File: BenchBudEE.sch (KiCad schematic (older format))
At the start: 0 parts

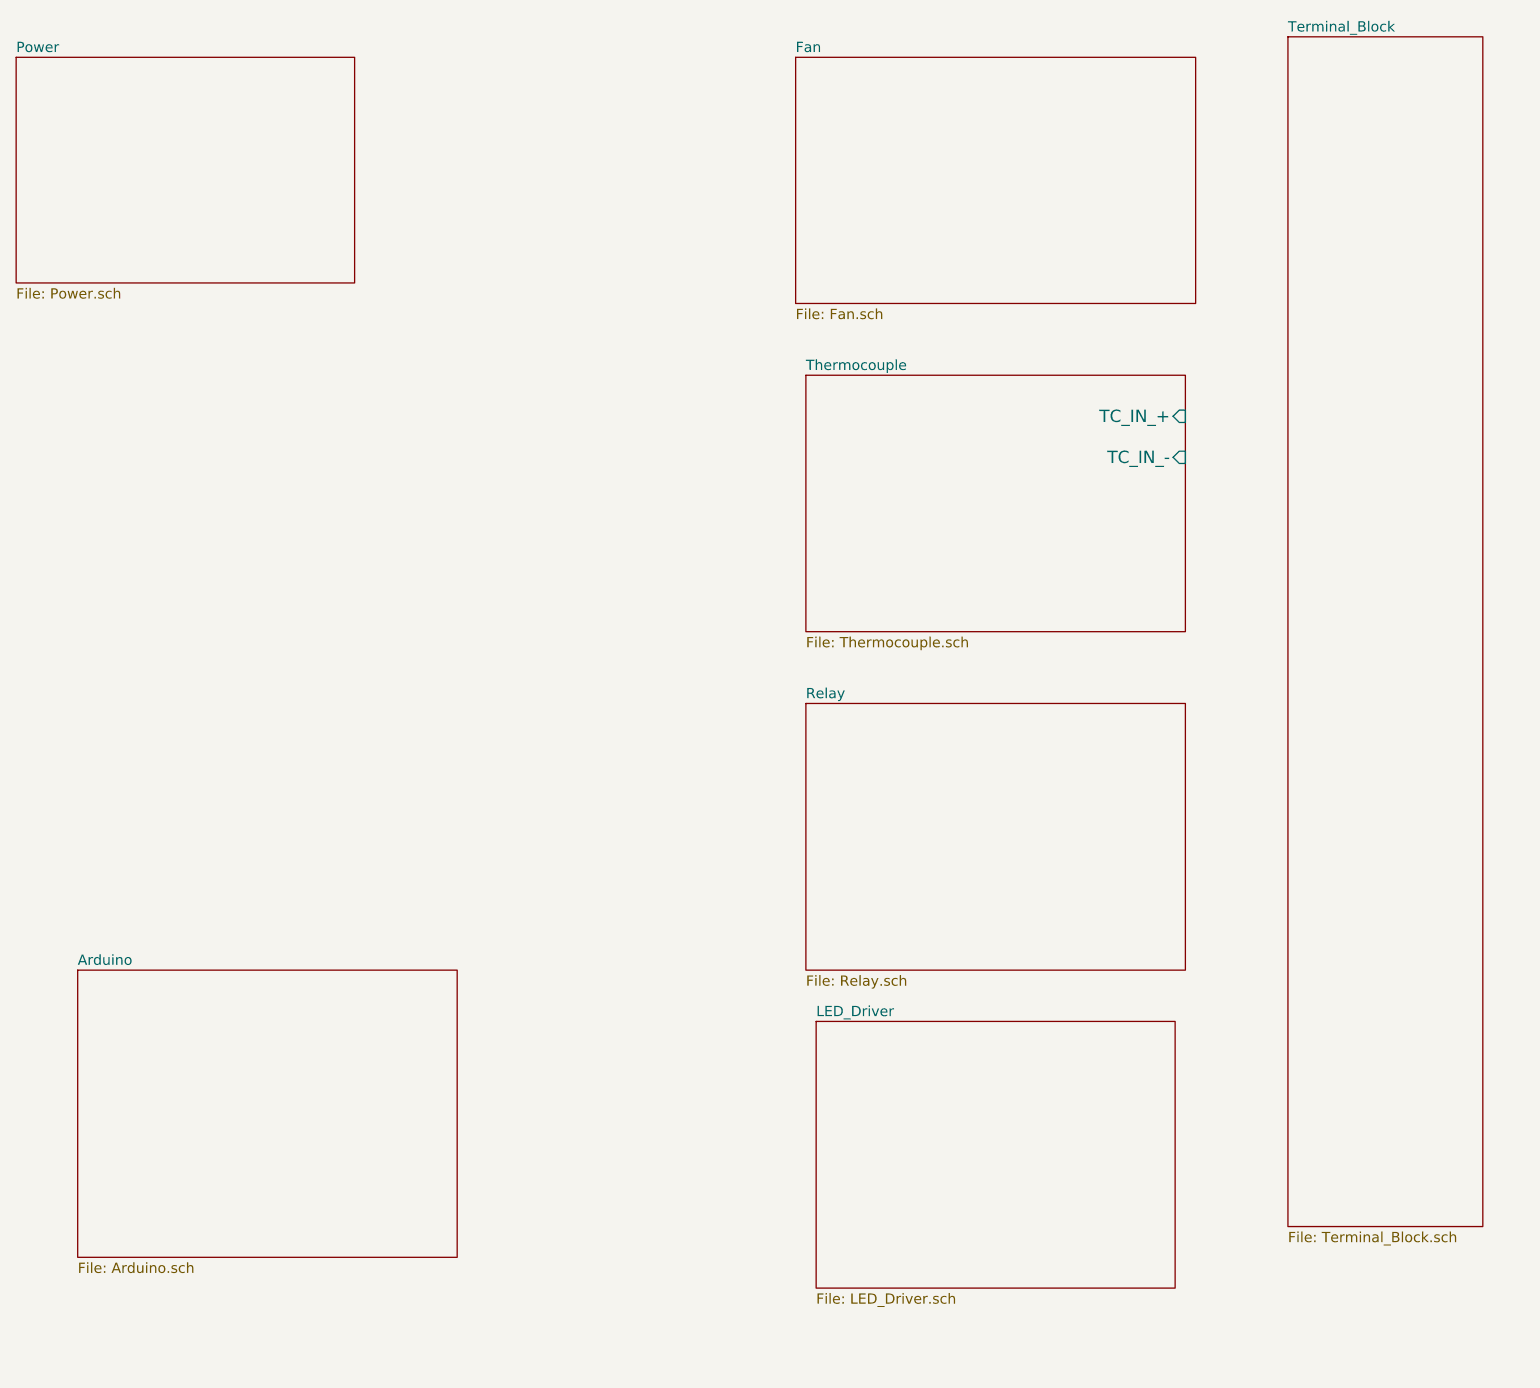
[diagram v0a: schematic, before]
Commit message: Created inputs/outputs in hierarchical sheets
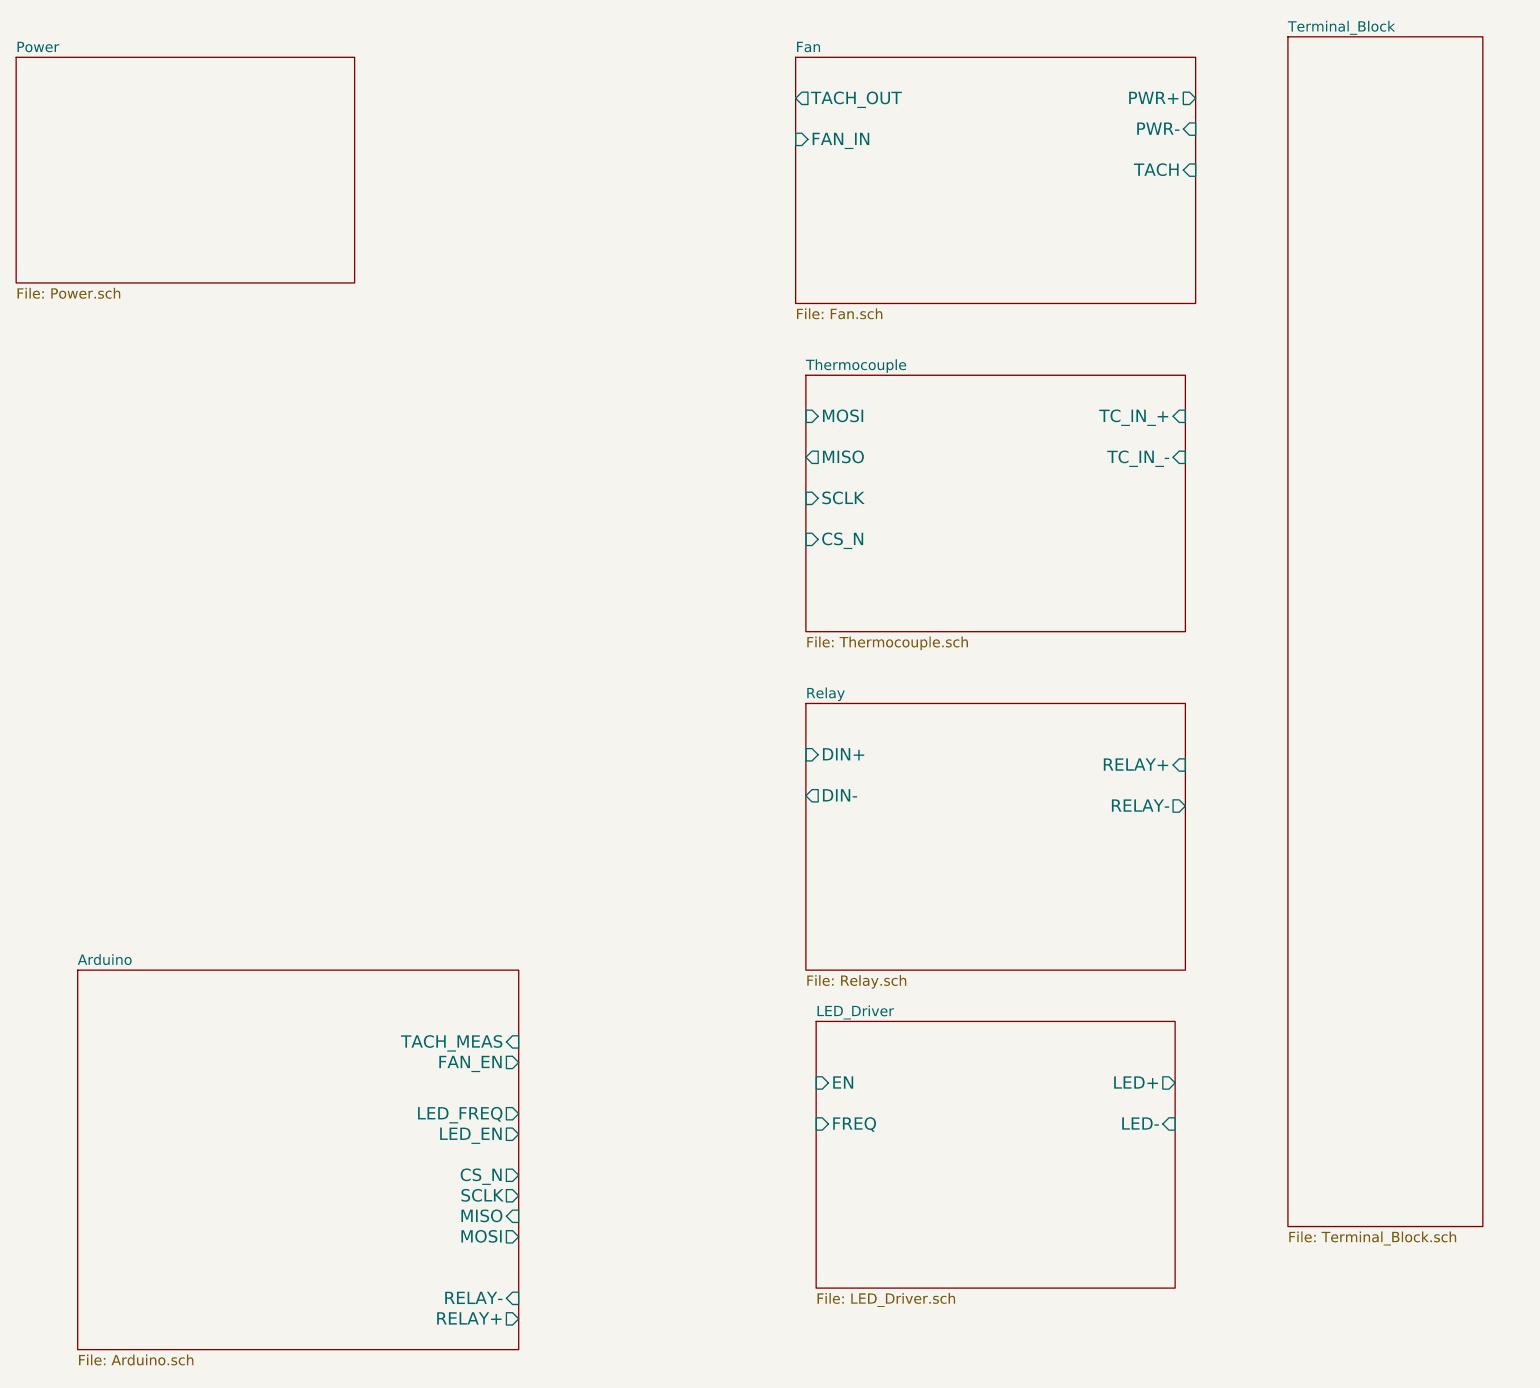
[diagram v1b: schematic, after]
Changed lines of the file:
@@
 $EndDescr
 $Sheet
-S 4000 5450 1850 1400
+S 4000 5450 2150 1850
 U 52EE0AAE
 F0 "Arduino" 50
 F1 "Arduino.sch" 50
+F2 "RELAY+" O R 6150 7150 60
+F3 "RELAY-" I R 6150 7050 60
+F4 "MOSI" O R 6150 6750 60
+F5 "MISO" I R 6150 6650 60
+F6 "SCLK" O R 6150 6550 60
+F7 "CS_N" O R 6150 6450 60
+F8 "LED_EN" O R 6150 6250 60
+F9 "LED_FREQ" O R 6150 6150 60
+F10 "FAN_EN" O R 6150 5900 60
+F11 "TACH_MEAS" I R 6150 5800 60
 $EndSheet
 $Sheet
@@
 F2 "TC_IN_+" I R 9400 2750 60
 F3 "TC_IN_-" I R 9400 2950 60
+F4 "MOSI" I L 7550 2750 60
+F5 "MISO" O L 7550 2950 60
+F6 "SCLK" I L 7550 3150 60
+F7 "CS_N" I L 7550 3350 60
 $EndSheet
 $Sheet
@@
 F0 "Relay" 50
 F1 "Relay.sch" 50
+F2 "DIN+" I L 7550 4400 60
+F3 "DIN-" O L 7550 4600 60
+F4 "RELAY+" I R 9400 4450 60
+F5 "RELAY-" O R 9400 4650 60
 $EndSheet
 $Sheet
@@
 F0 "LED_Driver" 50
 F1 "LED_Driver.sch" 50
+F2 "EN" I L 7600 6000 60
+F3 "FREQ" I L 7600 6200 60
+F4 "LED+" O R 9350 6000 60
+F5 "LED-" I R 9350 6200 60
 $EndSheet
 $Sheet
@@
 F0 "Fan" 50
 F1 "Fan.sch" 50
+F2 "PWR+" O R 9450 1200 60
+F3 "PWR-" I R 9450 1350 60
+F4 "TACH_OUT" O L 7500 1200 60
+F5 "FAN_IN" I L 7500 1400 60
+F6 "TACH" I R 9450 1550 60
 $EndSheet
 $Sheet

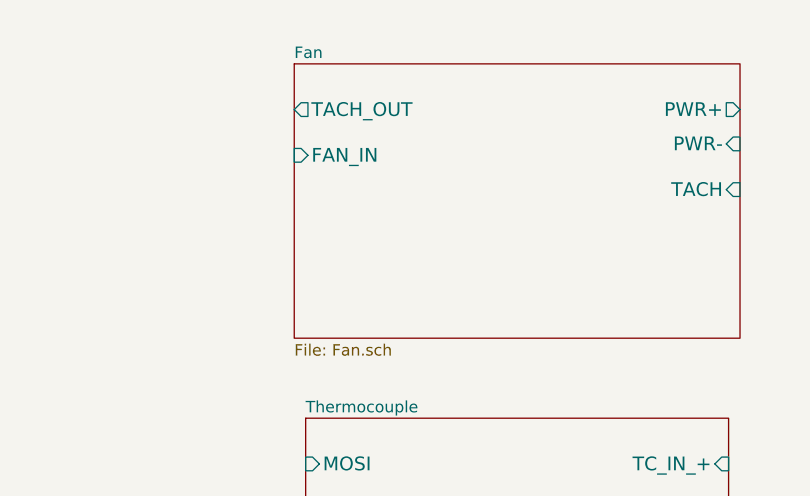
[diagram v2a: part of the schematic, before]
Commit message: Created first schematic for Fan Driver module
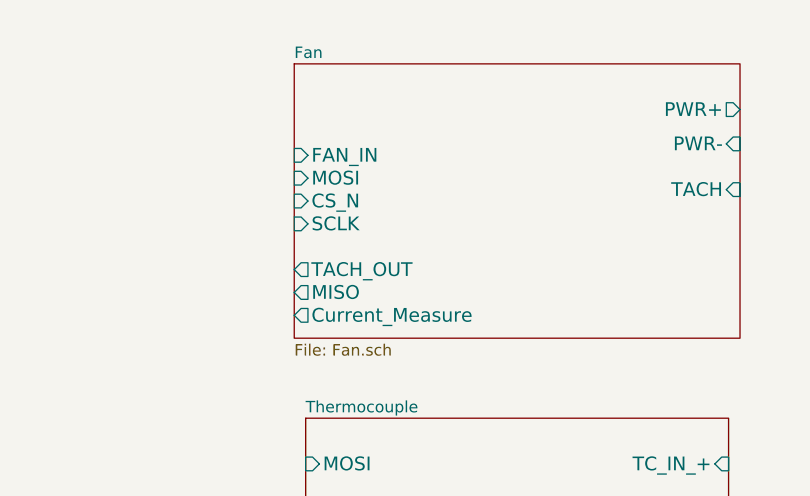
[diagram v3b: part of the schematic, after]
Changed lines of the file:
@@
 Sheet 1 8
 Title ""
-Date "7 feb 2014"
+Date "8 feb 2014"
 Rev ""
 Comp ""
@@
 F2 "PWR+" O R 9450 1200 60
 F3 "PWR-" I R 9450 1350 60
-F4 "TACH_OUT" O L 7500 1200 60
+F4 "TACH_OUT" O L 7500 1900 60
 F5 "FAN_IN" I L 7500 1400 60
 F6 "TACH" I R 9450 1550 60
+F7 "Current_Measure" O L 7500 2100 60
+F8 "MOSI" I L 7500 1500 60
+F9 "MISO" O L 7500 2000 60
+F10 "CS_N" I L 7500 1600 60
+F11 "SCLK" I L 7500 1700 60
 $EndSheet
 $Sheet
